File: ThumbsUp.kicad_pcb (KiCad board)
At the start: 2 copper layers, 250.8 x 270.5 mm, 172 parts, among them IC1 RP2040, IC2 W25Q128JVSIM, IC3 RP2040, IC4 W25Q128JVSIM, J1 Conn_01x04_Male, J10 Raiser_Male, J11 Raiser_Female, J12 Raiser_Male, J13 Raiser_Female, J14 Raiser_Male, J15 Raiser_Female, J16 Raiser_Male, J17 Raiser_Female, J18 Raiser_Male, J19 Raiser_Female, J2 Conn_01x04_Male, J20 Conn_01x04_Female, J21 Conn_01x04_Female, J22 Conn_01x04_Female, J23 Conn_01x04_Female, J24 Conn_01x04_Male, J25 Conn_01x04_Male, J26 Conn_01x04_Male, J27 Conn_01x04_Male, J28 Conn_01x04_Female, J29 Conn_01x04_Female, J3 Conn_01x04_Female, J30 Conn_01x04_Female, J31 Conn_01x04_Female, J32 USB_C_Receptacle_USB2.0, J33 Raiser_Male, J34 Raiser_Female, J35 Raiser_Male, J36 STX-3501-3N, J37 USB_C_Receptacle_USB2.0, J38 Raiser_Female, J39 Raiser_Male, J4 Conn_01x04_Male, J40 Raiser_Female, J41 Raiser_Male, J42 Raiser_Female, J43 Raiser_Male, J44 Raiser_Female, J45 Raiser_Male, J46 STX-3501-3N, J47 Raiser_Female, J48 Raiser_Male, J49 Raiser_Female, J5 Conn_01x04_Female, J50 Raiser_Male, J51 Raiser_Female, J52 Raiser_Male, J6 Conn_01x04_Male, J7 Conn_01x04_Male, J8 Conn_01x04_Male, J9 Raiser_Female, U1 NCP1117-3.3_SOT223, U2 NCP1117-3.3_SOT223, Y1 ABLS-12.000MHZ-B4-T, Y2 ABLS-12.000MHZ-B4-T

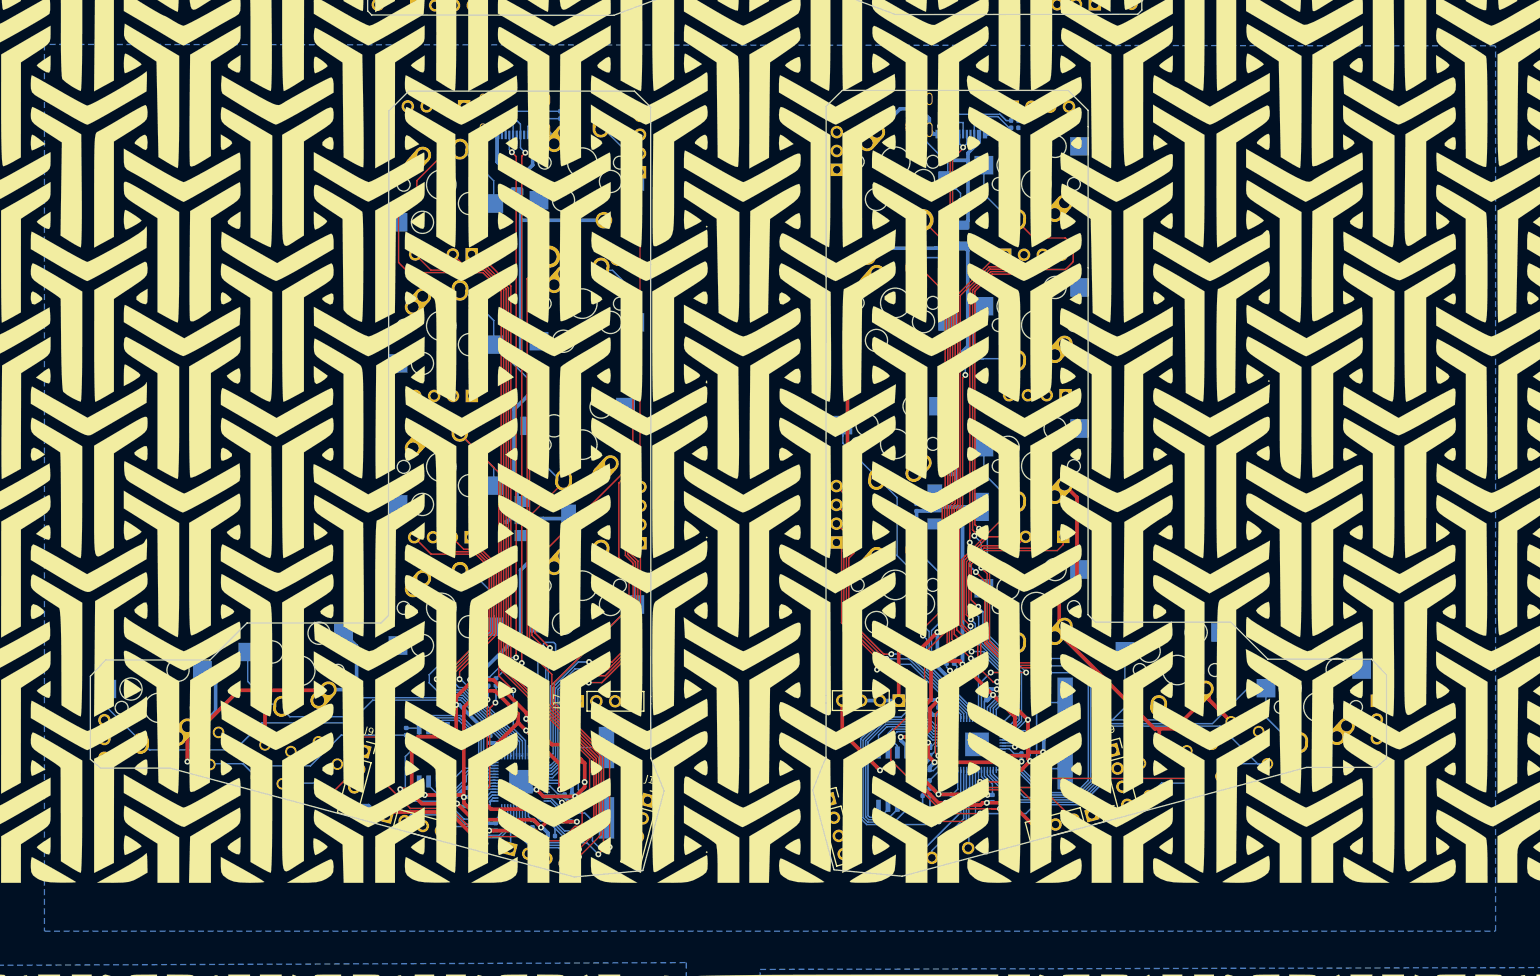
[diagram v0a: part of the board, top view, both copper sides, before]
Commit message: Removed fill zone from the middle layer - they were shortening the areas under MCU and USB connectors.
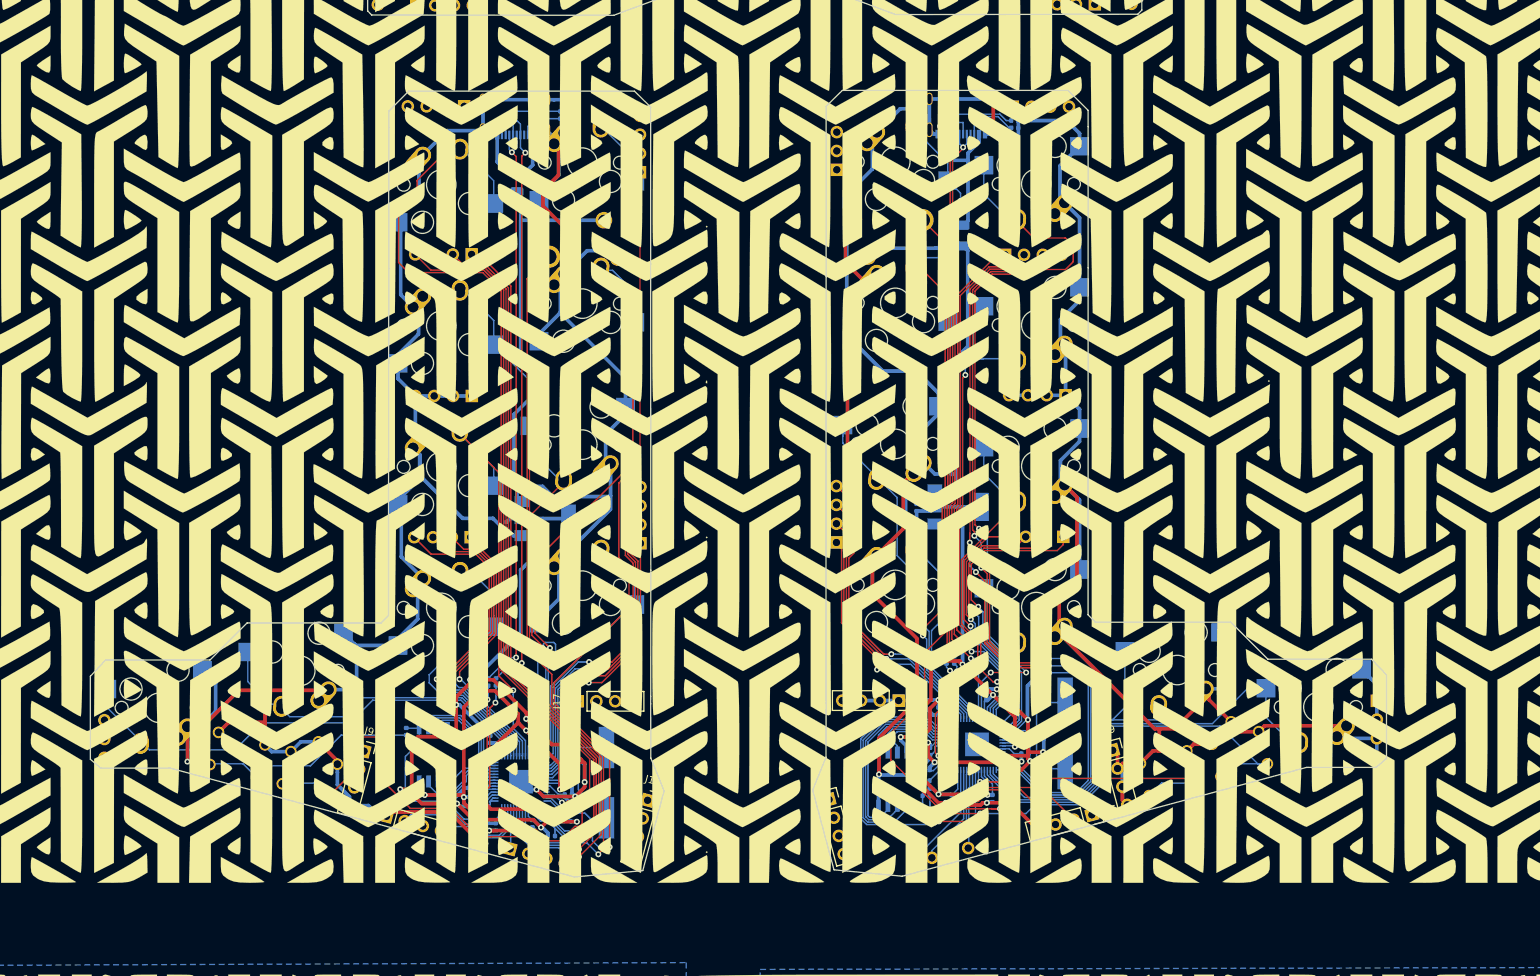
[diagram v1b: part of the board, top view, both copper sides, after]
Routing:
- net L-BASE: track 429.5 -> 1015.2 mm, vias 34 -> 31
- removed copper zone on B.Cu, net L-BASE

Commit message: Replacing voltage regulators with available parts - PCBs updated.
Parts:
- removed G*** (x3): LOGO, Silkscreens:Crowfeet75
- C11, C18: value 10uF -> 100uF; footprint Capacitor_SMD:C_0402_1005Metric -> Capacitor_SMD:C_1210_3225Metric
- U1, U2: value NCP1117-3.3_SOT223 -> AMS1117-3.3_SOT223; footprint Package_TO_SOT_SMD:SOT-223-3_TabPin2 -> AMS1117-3.3:SOT229P700X180-4N
- moved C11 6.96 mm to (112.4, 434.2), turned to 90 degrees
- moved C18 2.29 mm to (164.1, 426.4), turned to 180 degrees
- moved R5 1.51 mm to (165.3, 423.8), turned to 180 degrees
- moved C8 1.48 mm to (170.1, 419.0)
- moved C9 1.42 mm to (113.5, 420.7)
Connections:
- IC1 pad 24: Net-(IC1-Pad24) -> (no net)
- IC1 pad 25: Net-(IC1-Pad25) -> (no net)
- IC3 pad 24: Net-(IC3-Pad24) -> (no net)
- IC3 pad 25: Net-(IC3-Pad25) -> (no net)
- J1 pad 2: Net-(J1-Pad2) -> (no net)
- J1 pad 3: Net-(J1-Pad3) -> (no net)
- J1 pad 4: Net-(J1-Pad4) -> (no net)
- J10 pad 1: Net-(J10-Pad1) -> (no net)
- J10 pad 2: Net-(J10-Pad2) -> (no net)
- J10 pad 3: Net-(J10-Pad3) -> (no net)
- J10 pad 4: Net-(J10-Pad4) -> (no net)
- J13 pad 1: Net-(J13-Pad1) -> (no net)
- J13 pad 2: Net-(J13-Pad2) -> (no net)
- J13 pad 3: Net-(J13-Pad3) -> (no net)
- J13 pad 4: Net-(J13-Pad4) -> (no net)
- J14 pad 1: Net-(J14-Pad1) -> (no net)
- J14 pad 2: Net-(J14-Pad2) -> (no net)
- J14 pad 3: Net-(J14-Pad3) -> (no net)
- J14 pad 4: Net-(J14-Pad4) -> (no net)
- J17 pad 1: Net-(J17-Pad1) -> (no net)
- J17 pad 2: Net-(J17-Pad2) -> (no net)
- J17 pad 3: Net-(J17-Pad3) -> (no net)
- J17 pad 4: Net-(J17-Pad4) -> (no net)
- J18 pad 1: Net-(J18-Pad1) -> (no net)
- J18 pad 2: Net-(J18-Pad2) -> (no net)
- J18 pad 3: Net-(J18-Pad3) -> (no net)
- J18 pad 4: Net-(J18-Pad4) -> (no net)
- J20 pad 1: Net-(J20-Pad1) -> (no net)
- J20 pad 2: Net-(J20-Pad2) -> (no net)
- J20 pad 3: Net-(J20-Pad3) -> (no net)
- J20 pad 4: Net-(J20-Pad4) -> (no net)
- J28 pad 1: Net-(J28-Pad1) -> (no net)
- J28 pad 2: Net-(J28-Pad2) -> (no net)
- J28 pad 3: Net-(J28-Pad3) -> (no net)
- J28 pad 4: Net-(J28-Pad4) -> (no net)
- J3 pad 3: Net-(J3-Pad3) -> (no net)
- J32 pad A8: Net-(J32-PadA8) -> (no net)
- J32 pad B8: Net-(J32-PadB8) -> (no net)
- J33 pad 1: Net-(J33-Pad1) -> (no net)
- J33 pad 2: Net-(J33-Pad2) -> (no net)
- J33 pad 3: Net-(J33-Pad3) -> (no net)
- J33 pad 4: Net-(J33-Pad4) -> (no net)
- J35 pad 1: Net-(J35-Pad1) -> (no net)
- J35 pad 2: Net-(J35-Pad2) -> (no net)
- J35 pad 3: Net-(J35-Pad3) -> (no net)
- J35 pad 4: Net-(J35-Pad4) -> (no net)
- J37 pad A8: Net-(J37-PadA8) -> (no net)
- J37 pad B8: Net-(J37-PadB8) -> (no net)
- J38 pad 1: Net-(J38-Pad1) -> (no net)
- J38 pad 2: Net-(J38-Pad2) -> (no net)
- J38 pad 3: Net-(J38-Pad3) -> (no net)
- J38 pad 4: Net-(J38-Pad4) -> (no net)
- J39 pad 2: Net-(J39-Pad2) -> (no net)
- J39 pad 3: Net-(J39-Pad3) -> (no net)
- J39 pad 4: Net-(J39-Pad4) -> (no net)
- J4 pad 3: Net-(J4-Pad3) -> (no net)
- J40 pad 1: Net-(J40-Pad1) -> (no net)
- J40 pad 2: Net-(J40-Pad2) -> (no net)
- J40 pad 3: Net-(J40-Pad3) -> (no net)
- J40 pad 4: Net-(J40-Pad4) -> (no net)
- J41 pad 1: Net-(J41-Pad1) -> (no net)
- J41 pad 2: Net-(J41-Pad2) -> (no net)
- J41 pad 3: Net-(J41-Pad3) -> (no net)
- J41 pad 4: Net-(J41-Pad4) -> (no net)
- J47 pad 1: Net-(J47-Pad1) -> (no net)
- J47 pad 2: Net-(J47-Pad2) -> (no net)
- J47 pad 3: Net-(J47-Pad3) -> (no net)
- J47 pad 4: Net-(J47-Pad4) -> (no net)
- J48 pad 1: Net-(J48-Pad1) -> (no net)
- J48 pad 2: Net-(J48-Pad2) -> (no net)
- J48 pad 3: Net-(J48-Pad3) -> (no net)
- J48 pad 4: Net-(J48-Pad4) -> (no net)
- J49 pad 1: Net-(J49-Pad1) -> (no net)
- J49 pad 2: Net-(J49-Pad2) -> (no net)
- J49 pad 3: Net-(J49-Pad3) -> (no net)
- J49 pad 4: Net-(J49-Pad4) -> (no net)
- J5 pad 1: Net-(J5-Pad1) -> (no net)
- J50 pad 1: Net-(J50-Pad1) -> (no net)
- J50 pad 2: Net-(J50-Pad2) -> (no net)
- J50 pad 3: Net-(J50-Pad3) -> (no net)
- J50 pad 4: Net-(J50-Pad4) -> (no net)
- J51 pad 1: Net-(J51-Pad1) -> (no net)
- J51 pad 2: Net-(J51-Pad2) -> (no net)
- J51 pad 3: Net-(J51-Pad3) -> (no net)
- J51 pad 4: Net-(J51-Pad4) -> (no net)
- J52 pad 1: Net-(J52-Pad1) -> (no net)
- J52 pad 2: Net-(J52-Pad2) -> (no net)
- J52 pad 3: Net-(J52-Pad3) -> (no net)
- J52 pad 4: Net-(J52-Pad4) -> (no net)
- J6 pad 1: Net-(J6-Pad1) -> (no net)
- J9 pad 1: Net-(J9-Pad1) -> (no net)
- J9 pad 2: Net-(J9-Pad2) -> (no net)
- J9 pad 3: Net-(J9-Pad3) -> (no net)
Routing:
- net L-BASE: track 1015.2 -> 1024.2 mm
- net K_7: track 133.1 -> 130.4 mm
- net K_8: track 106.5 -> 104.2 mm
- net +3V3: track 253.1 -> 254.2 mm
- net L-RING1: track 108.3 -> 108.9 mm

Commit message: Added silkscreen before generating Gerbers.
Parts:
- added G***: LOGO, Silkscreens:Crowfeet75, F.Cu at (141.1, 399.3)
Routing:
- net K_G: track 52.7 -> 55.6 mm
- net K_7: track 130.4 -> 133.1 mm
- net K_8: track 104.2 -> 106.5 mm
- net K_T: track 85.0 -> 86.0 mm
- net L-TIP: track 99.6 -> 100.5 mm
- net L-RING1: track 108.9 -> 108.3 mm
- net D+: track 80.5 -> 81.0 mm
